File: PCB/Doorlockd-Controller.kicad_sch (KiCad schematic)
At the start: 59 parts, among them J1 MilkV P43 (3.3V for VCCB), J10 Power Out 1, J11 DC in, J12 IO 3, J13 Debug UART, J14 IO 4, J15 Power Out 2, J16 to extra screw conn., J18 GPIO only MilkV 1.8V, J19 3V 5V Vin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

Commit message: Replace STU60N3LH5 FET with STD12NF06L-1
The former is not available anymore since a while, the latter is
another IPAK FET with similar specs.
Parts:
- Q2, Q5: value STU60N3LH5 -> STD12NF06L-1
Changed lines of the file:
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@@
 			)
 		)
-		(property "Value" "STU60N3LH5"
+		(property "Value" "STD12NF06L-1"
 			(at 139.7 129.032 0)
 			(effects
@@
 			)
 		)
-		(property "Value" "STU60N3LH5"
+		(property "Value" "STD12NF06L-1"
 			(at 54.61 129.032 0)
 			(effects

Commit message: Improve mounting hole accuracy
Turns out these holes were actually 26.565 degrees (atan(0.5)), not 22.5.
This fixes the footprint to angle the pad at 26.5 and puts the courtyard
and user comments figures in the exactly correct spot.

This also renames the footprint, switching from specifying the angle
(which would be inexact) to the center offset of the second hole.
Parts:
- H1, H2, H3, H4: footprint MountingHole_3.2x4.32mm_Oval_22.5deg:MountingHole_3.2x4.32mm_Oval_22.5deg -> MountingHole_Dual_3.2mm_M3_Offset1x0.5mm:MountingHole_Dual_3.2mm_M3_Offset1x0.5mm
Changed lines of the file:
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@@
 			)
 		)
-		(property "Footprint" "MountingHole_3.2x4.32mm_Oval_22.5deg:MountingHole_3.2x4.32mm_Oval_22.5deg"
+		(property "Footprint" "MountingHole_Dual_3.2mm_M3_Offset1x0.5mm:MountingHole_Dual_3.2mm_M3_Offset1x0.5mm"
 			(at 254 67.31 0)
 			(effects
@@
 			)
 		)
-		(property "Footprint" "MountingHole_3.2x4.32mm_Oval_22.5deg:MountingHole_3.2x4.32mm_Oval_22.5deg"
+		(property "Footprint" "MountingHole_Dual_3.2mm_M3_Offset1x0.5mm:MountingHole_Dual_3.2mm_M3_Offset1x0.5mm"
 			(at 246.38 67.31 0)
 			(effects
@@
 			)
 		)
-		(property "Footprint" "MountingHole_3.2x4.32mm_Oval_22.5deg:MountingHole_3.2x4.32mm_Oval_22.5deg"
+		(property "Footprint" "MountingHole_Dual_3.2mm_M3_Offset1x0.5mm:MountingHole_Dual_3.2mm_M3_Offset1x0.5mm"
 			(at 246.38 62.23 0)
 			(effects
@@
 			)
 		)
-		(property "Footprint" "MountingHole_3.2x4.32mm_Oval_22.5deg:MountingHole_3.2x4.32mm_Oval_22.5deg"
+		(property "Footprint" "MountingHole_Dual_3.2mm_M3_Offset1x0.5mm:MountingHole_Dual_3.2mm_M3_Offset1x0.5mm"
 			(at 254 62.23 0)
 			(effects

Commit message: Change license to CERN-OHL-P v2+
Also makes some other small tweaks to the title sheet.
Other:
- title: Doorlockd-Controller (Rock pi-S/Milk-V duo S) -> Doorlockd Controller PCB
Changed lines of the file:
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@@
 	(paper "A4")
 	(title_block
-		(title "Doorlockd-Controller (Rock pi-S/Milk-V duo S)")
+		(title "Doorlockd Controller PCB")
 		(date "2025-06-17")
-		(rev "v2.0")
-		(comment 1 "author: Diederik Hamelink")
-		(comment 2 "CC BY 4.0")
-		(comment 3 "github.com/doorlockd")
-		(comment 4 "de WAR")
+		(comment 1 "Copyright 2025 Diederik Hamelink (wie-niet) & Matthijs Kooijman")
+		(comment 2 "Licensed under CERN-OHL-P v2 or any later version")
 	)
 	(text "Generic In/Out \ninput: C 1uF, R 220\noutput C none, R (depends on LED / ?)"
@@
 	)
 	(image
-		(at 265.43 173.99)
+		(at 265.43 171.45)
 		(scale 2)
 		(data "iVBORw0KGgoAAAANSUhEUgAAAEAAAABACAYAAACqaXHeAAAABHNCSVQICAgIfAhkiAAAA8JJREFU"
@@
 	(symbol
 		(lib_id "Graphic:Logo_Open_Hardware_Small")
-		(at 275.59 175.26 0)
+		(at 275.59 172.72 0)
 		(unit 1)
 		(exclude_from_sim yes)
@@
 		(dnp no)
 		(property "Reference" "#LOGO1"
-			(at 275.59 168.275 0)
+			(at 275.59 165.735 0)
 			(effects
 				(font
@@
 		)
 		(property "Value" "Logo_Open_Hardware_Small"
-			(at 275.59 180.975 0)
+			(at 275.59 178.435 0)
 			(effects
 				(font
@@
 		)
 		(property "Footprint" ""
-			(at 275.59 175.26 0)
+			(at 275.59 172.72 0)
 			(effects
 				(font
@@
 		)
 		(property "Datasheet" "~"
-			(at 275.59 175.26 0)
+			(at 275.59 172.72 0)
 			(effects
 				(font
@@
 		)
 		(property "Description" "Open Hardware logo, small"
-			(at 275.59 175.26 0)
+			(at 275.59 172.72 0)
 			(effects
 				(font

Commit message: Change LED resistors to 220
This reduces LED current a bit, and reduces BOM count.
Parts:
- R1, R4: value 100 -> 220
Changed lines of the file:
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@@
 			)
 		)
-		(property "Value" "100"
+		(property "Value" "220"
 			(at 33.02 132.334 90)
 			(effects
@@
 			)
 		)
-		(property "Value" "100"
+		(property "Value" "220"
 			(at 118.11 132.334 90)
 			(effects

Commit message: Use correct IPAK footprint
This used the SIPAK footprint, but that is slightly different (and has
no 3D model), so use the IPAK/TO-251-3 footprint instead.
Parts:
- Q2, Q5: footprint Package_TO_SOT_THT:SIPAK_Vertical -> Package_TO_SOT_THT:TO-251-3_Vertical
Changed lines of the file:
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@@
 			)
 		)
-		(property "Footprint" "Package_TO_SOT_THT:SIPAK_Vertical"
+		(property "Footprint" "Package_TO_SOT_THT:TO-251-3_Vertical"
 			(at 140.97 124.46 0)
 			(effects
@@
 			)
 		)
-		(property "Footprint" "Package_TO_SOT_THT:SIPAK_Vertical"
+		(property "Footprint" "Package_TO_SOT_THT:TO-251-3_Vertical"
 			(at 55.88 124.46 0)
 			(effects

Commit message: Improve note about audio connector
Turns out the two mentioned connectors have the same footprint, but are
not pin-compatible (ring and sleeve are swapped).
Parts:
- J5: Note Lumberg 1503 30 and 07 are pin-compatible -> Lumberg 1503 30 and 07 have same footprint (but different p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
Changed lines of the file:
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@@
 			)
 		)
-		(property "Note" "Lumberg 1503 30 and 07 are pin-compatible"
+		(property "Note" "Lumberg 1503 30 and 07 have same footprint (but different pinout!)"
 			(at 160.02 22.86 0)
 			(effects

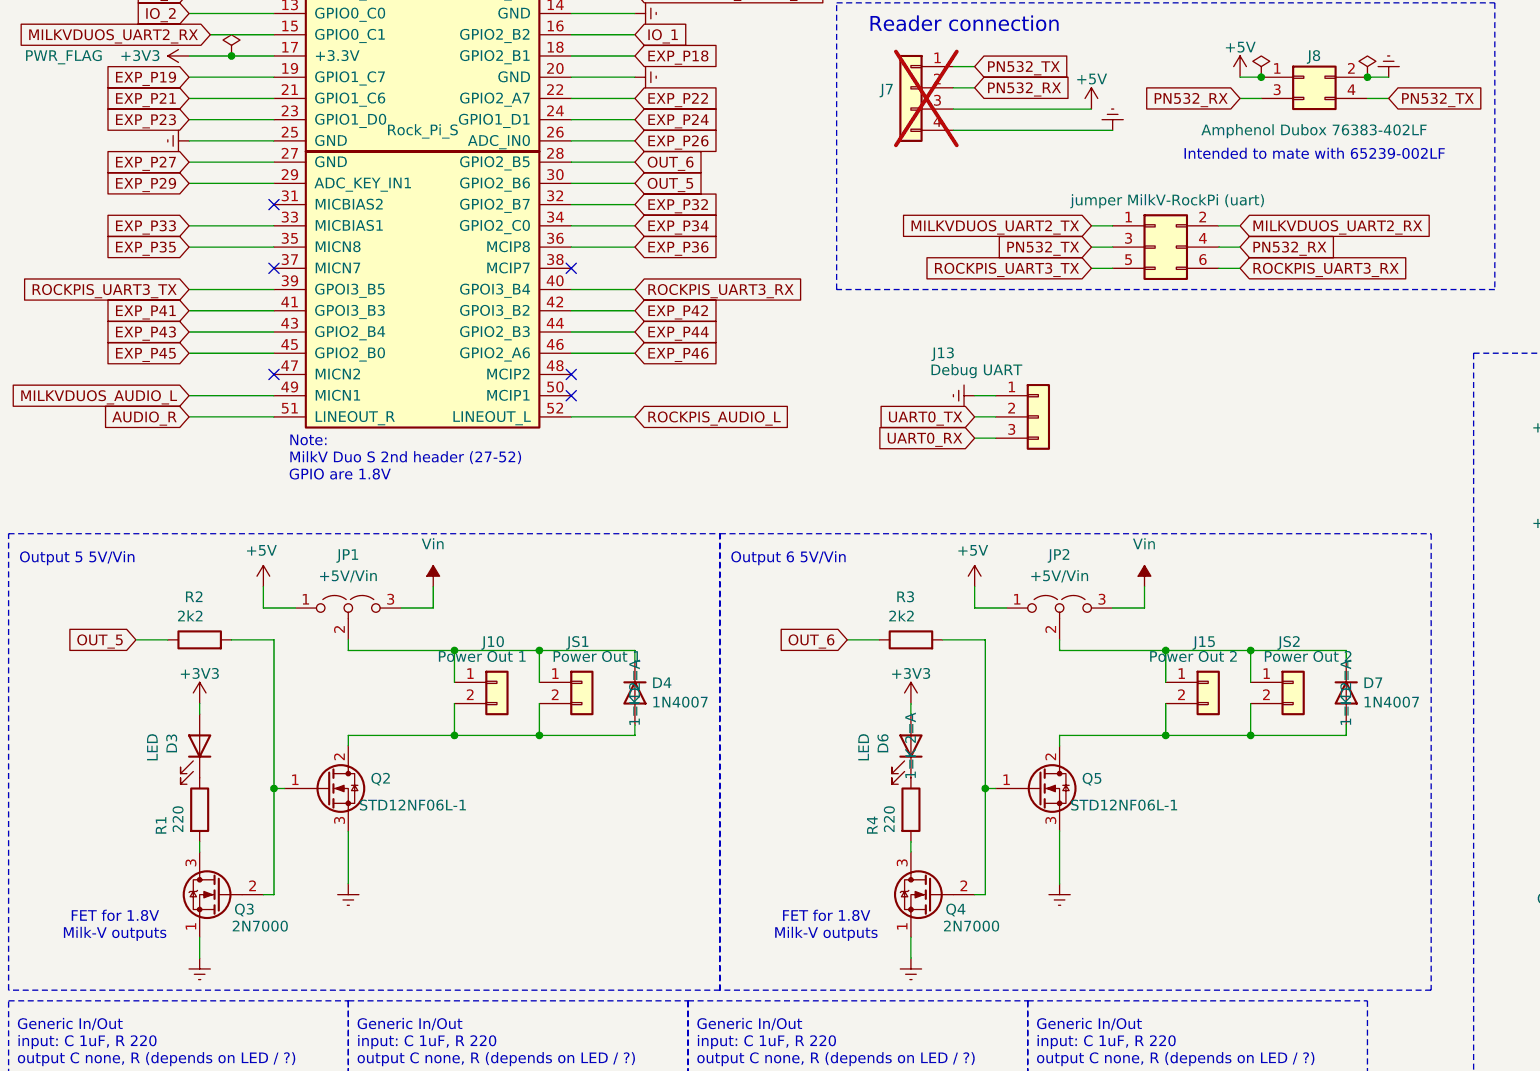
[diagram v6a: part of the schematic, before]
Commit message: Swap output 5 and 6
The were accidentally mislabeled in the silkscreen. To preserve the
logical order on the PCB, the silk is unchanged, but the schematic is
changed to swap them instead.
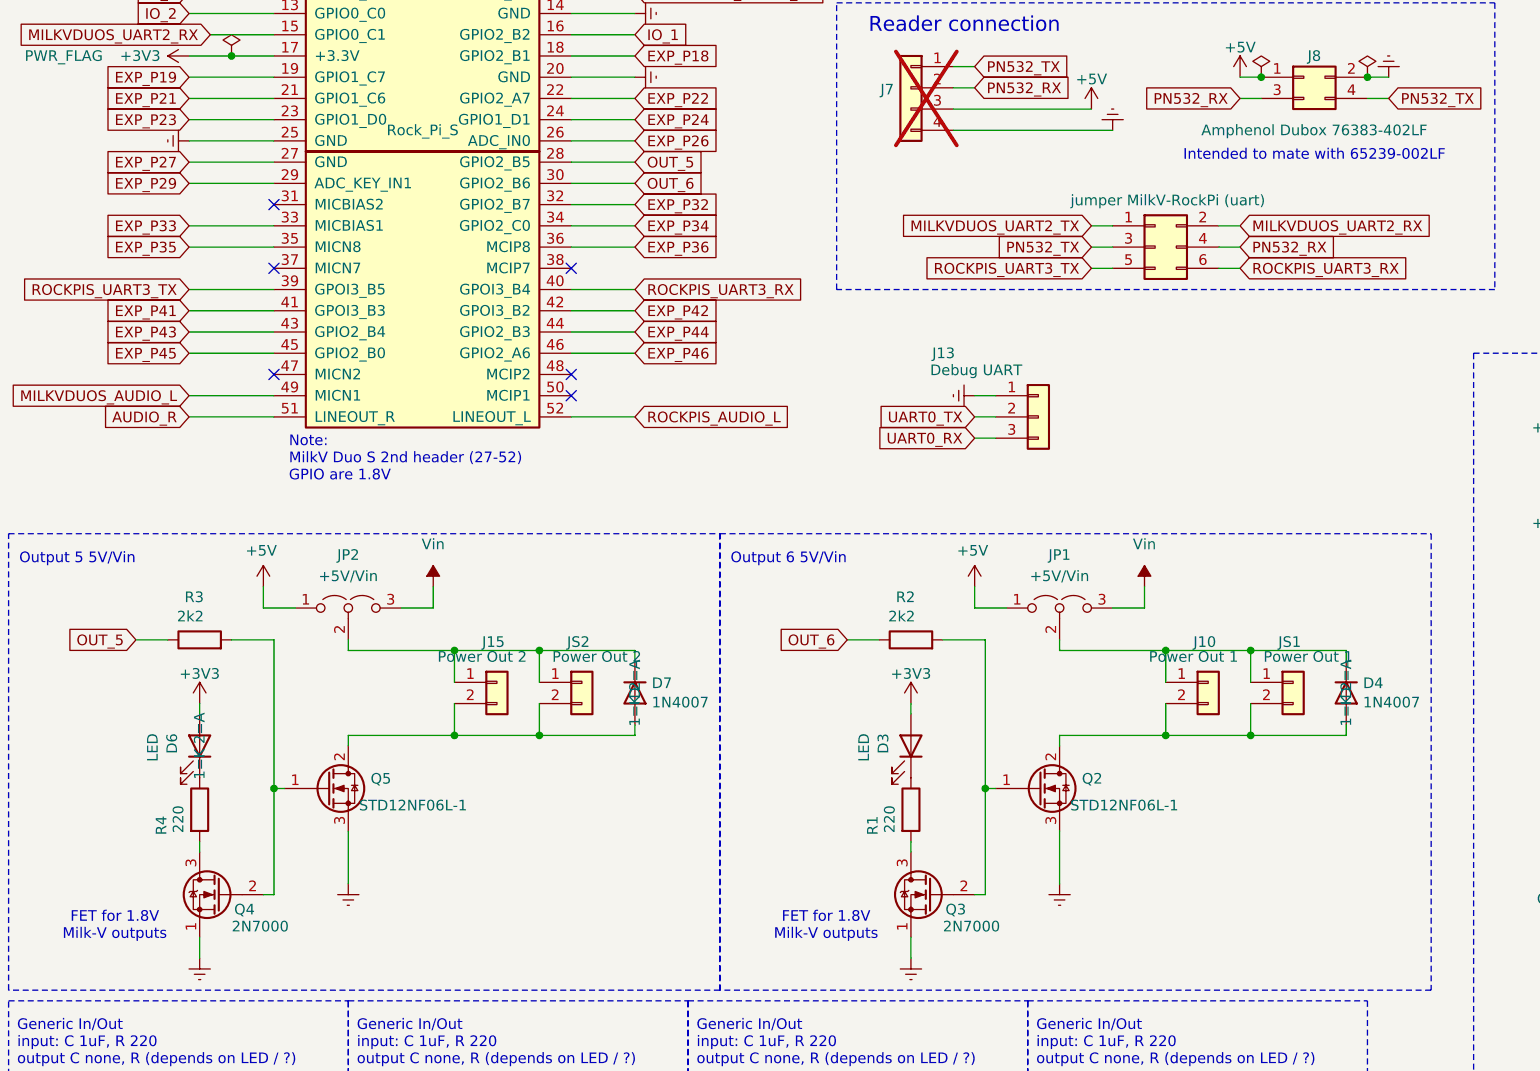
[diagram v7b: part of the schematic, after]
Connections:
- net OUT_5: now also R3.1, U2.28 (GPIO2_B5); no longer R2.1, U2.30 (GPIO2_B6)
- net OUT_6: now also R2.1, U2.30 (GPIO2_B6); no longer R3.1, U2.28 (GPIO2_B5)
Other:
- moved on the sheet: D3, D4, D6, D7, J10, J15, JP1, JP2, JS1, JS2, Q2, Q3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

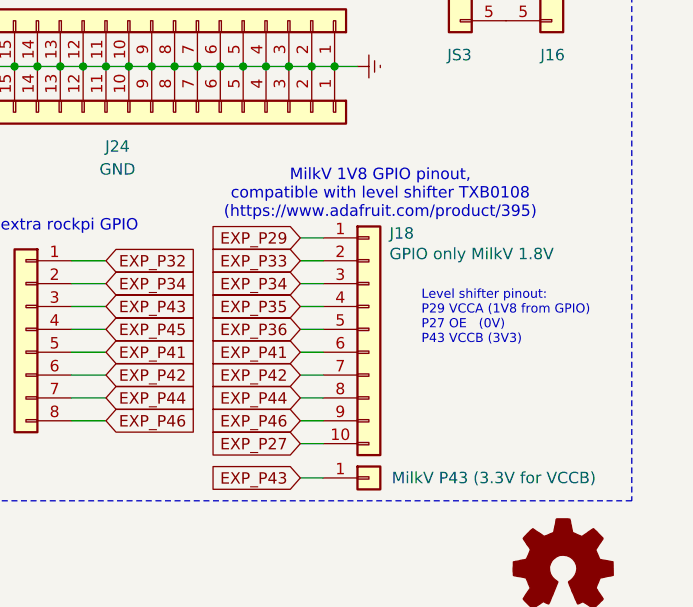
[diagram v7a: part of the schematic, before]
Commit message: Improve level shifter note in schematic
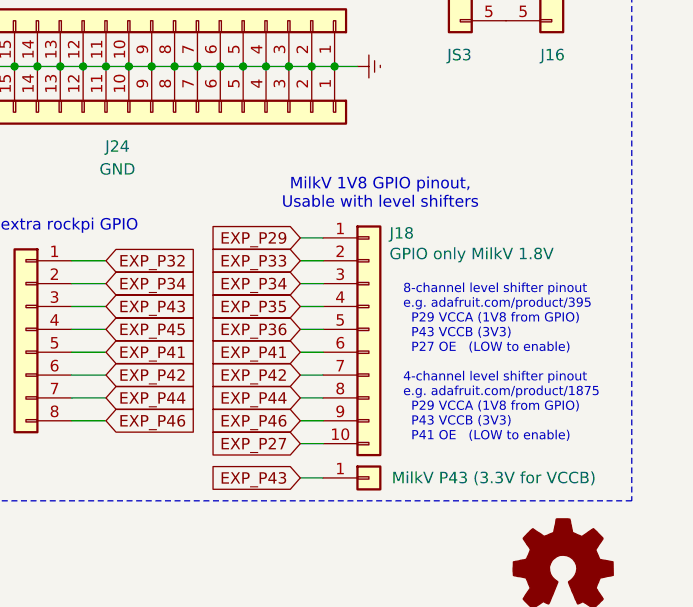
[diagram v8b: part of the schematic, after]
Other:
- note added: "8-channel level shifter pinout e.g. adafruit.com/product/395 P29 VCCA (1V8 from GPIO) P43 VCCB (3V3) P27 OE (LOW to enable) 4-channel level shifter pinout e.g. adafruit.com/product/1875 P29 VCCA (1V8 from GPIO) P43 VCCB (3V3) P41 OE (LOW to enable)"
- note added: "MilkV 1V8 GPIO pinout, Usable with level shifters"
- note removed: "Level shifter pinout: P29 VCCA (1V8 from GPIO) P27 OE (0V) P43 VCCB (3V3)"
- note removed: "MilkV 1V8 GPIO pinout, compatible with level shifter TXB0108 (https://www.adafruit.com/product/395)"
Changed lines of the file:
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@@
 		)
 	)
-	(text "MilkV 1V8 GPIO pinout, \ncompatible with level shifter TXB0108 \n(https://www.adafruit.com/product/395)"
+	(text "MilkV 1V8 GPIO pinout, \nUsable with level shifters"
 		(exclude_from_sim no)
 		(at 255.27 131.064 0)
@@
 		)
 	)
-	(text "Level shifter pinout:\nP29 VCCA (1V8 from GPIO)\nP27 OE   (0V)\nP43 VCCB (3V3)"
+	(text "8-channel level shifter pinout\ne.g. adafruit.com/product/395\n  P29 VCCA (1V8 from GPIO)\n  P43 VCCB (3V3)\n  P27 OE   (LOW to enable)\n\n4-channel level shifter pinout\ne.g. adafruit.com/product/1875\n  P29 VCCA (1V8 from GPIO)\n  P43 VCCB (3V3)\n  P41 OE   (LOW to enable)\n"
 		(exclude_from_sim no)
-		(at 259.842 144.78 0)
+		(at 257.81 149.86 0)
 		(effects
 			(font
